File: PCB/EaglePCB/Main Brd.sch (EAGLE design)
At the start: 9 parts, among them J1 1909763-1, J2 1909763-1, U1 ATWINC1500-MR210PB1952-T, U2 ENC28J60-I/SP, U3 MSP430FR2355TDBTRDBT0038A_M, U4 SX1272IMLTRT, U5 SX1272IMLTRT, U6 ARJM11C7-114-BA-EW2

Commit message: LoRa Antenna + Ethernet routing
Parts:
- removed J2: 1909763-1, 473:1909763-1
- added 10NH-ANT1, 10NH-ANT2, C1: (no value), microbuilder:CAP_CERAMIC0402
- added ANT1-ANT2\, ANT1-ANT2\1: 8.2nH, microbuilder:INDUCTOR_0402
- added ANT1-GND, ANT1-GND1, ANT2-GND, ANT2-GND1, ANT2-GND2, ANT2-GND3: 4.7pF, microbuilder:CAP_CERAMIC0402
- added ANT2-ANT1, ANT2-ANT3: 7.5nH, microbuilder:INDUCTOR_0402
- added J3: 1909763-1, 473:1909763-1
- added L2: (no value), microbuilder:INDUCTOR_0402
- added R1: (no value), microbuilder:RESISTOR0402
- added RFI-GND, RFI-GND1: 5.6 nH, microbuilder:INDUCTOR_0402
- added RFI-RFO, RFI-RFO1: 1.5pF 50v Cer, microbuilder:CAP_CERAMIC0402
- added RFO-33PF, RFO-33PF1: 10nH, microbuilder:INDUCTOR_0402
- added RFO-VR_PA, RFO-VR_PA1, VR_PA-PA_BOOST, VR_PA-PA_BOOST1: 33nH, microbuilder:INDUCTOR_0402
- renumbered U4 to LORA2, U5 to LORA1
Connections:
- new net ANT1: 10NH-ANT1.P$1, ANT1-ANT2\.2, ANT1-GND.P$2
- new net ANT1-2: 10NH-ANT2.P$1, ANT1-ANT2\1.2, ANT1-GND1.P$2
- new net ANT2: ANT1-ANT2\.1, ANT2-ANT3.2, ANT2-GND.P$2
- new net ANT2-2: ANT1-ANT2\1.1, ANT2-ANT1.2, ANT2-GND2.P$2
- new net ANT3: ANT2-ANT3.1, ANT2-GND1.P$2, J1.SIG
- new net ANT3-2: ANT2-ANT1.1, ANT2-GND3.P$2, J3.SIG
- new net GND: ANT1-GND.P$1, ANT1-GND1.P$1, ANT2-GND.P$1, ANT2-GND1.P$1, ANT2-GND2.P$1, ANT2-GND3.P$1, J1.GND, J1.GND_2, J3.GND, J3.GND_2, LORA1.GND, LORA1.GND_2, LORA1.GND_3, LORA1.GND_4, LORA2.GND, LORA2.GND_2, LORA2.GND_3, LORA2.GND_4, RFI-GND.2, RFI-GND1.2
- new net N$1: 10NH-ANT1.P$2, RFO-33PF.1
- new net N$2: 10NH-ANT2.P$2, RFO-33PF1.1
- new net PA_BOOST: LORA1.PA_BOOST, VR_PA-PA_BOOST.1
- new net PA_BOOST2: LORA2.PA_BOOST, VR_PA-PA_BOOST1.1
- new net RFI: LORA1.RFI, RFI-GND.1, RFI-RFO.P$1
- new net RFI2: LORA2.RFI, RFI-GND1.1, RFI-RFO1.P$1
- new net RFO: LORA1.RFO, RFI-RFO.P$2, RFO-33PF.2, RFO-VR_PA.2
- new net RFO2: LORA2.RFO, RFI-RFO1.P$2, RFO-33PF1.2, RFO-VR_PA1.2
- new net VR_PA: LORA1.VR_PA, RFO-VR_PA.1, VR_PA-PA_BOOST.2
- new net VR_PA2: LORA2.VR_PA, RFO-VR_PA1.1, VR_PA-PA_BOOST1.2
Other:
- moved on the sheet: J1, U1

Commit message: updated ethernet
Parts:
- added LEDG, LEDY: (no value), microbuilder:RESISTOR0402
- added RD-GND, RD-GND1: 0.1 uF, microbuilder:CAP_CERAMIC0402
- added RDM-GND, RDM-GND1: 49.9 Ohm', microbuilder:RESISTOR0402
- added RDP-GND, RDP-GND1: 49.9 Ohm, microbuilder:RESISTOR0402
- added TCT-3V3: (no value), microbuilder:FERRITE
- added U$1: NC_MARKER, NC_MARKER:NC_MARKER
- added VC2ETH-GND, VC2PETH-GND: 75 Ohm, microbuilder:RESISTOR0402
- added VC2ETH-GNDC, VC2PETH-GNDC: 1nF, microbuilder:CAP_CERAMIC0402
- added VCAPCLOSE: 10 uF, microbuilder:CAP_CERAMIC0805
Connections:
- new net 3V3: LEDG.2, LEDY.2, TCT-3V3.P$2
- new net LEDGN: U2.LEDA, U6.LED_3
- new net LEDYN: U6.LED
- new net LEDYP: U2.LEDB
- new net N$3: U$1.P$1, U6.RCT
- new net N$4: U2.VCAP, VCAPCLOSE.P$2
- new net N$5: VC2ETH-GND.1, VC2ETH-GNDC.P$2
- new net N$6: VC2PETH-GND.1, VC2PETH-GNDC.P$2
- new net N$7: LEDY.1, U6.LED_4
- new net N$8: RD-GND.P$1, RDM-GND.1, RDP-GND.1
- new net N$9: LEDG.1, U6.LED_2
- new net RDM: RDM-GND.2, U2.TPIN-, U6.RD-
- new net RDP: RDP-GND.2, U2.TPIN+, U6.RD+
- new net TDC: RD-GND1.P$1, RDM-GND1.1, RDP-GND1.1, TCT-3V3.P$1, U6.TCT
- new net TDM: RDM-GND1.2, U2.TPOUT-, U6.TD-
- new net TDP: RDP-GND1.2, U2.TPOUT+, U6.TD+
- new net VC2ETH: U6.VC2-, VC2ETH-GND.2
- new net VC2PETH: U6.VC2+, VC2PETH-GND.2
- net GND: now also RD-GND.P$2, RD-GND1.P$2, U6.VC1+, U6.VC1-, VC2ETH-GNDC.P$1, VC2PETH-GNDC.P$1, VCAPCLOSE.P$1
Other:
- moved on the sheet: U6

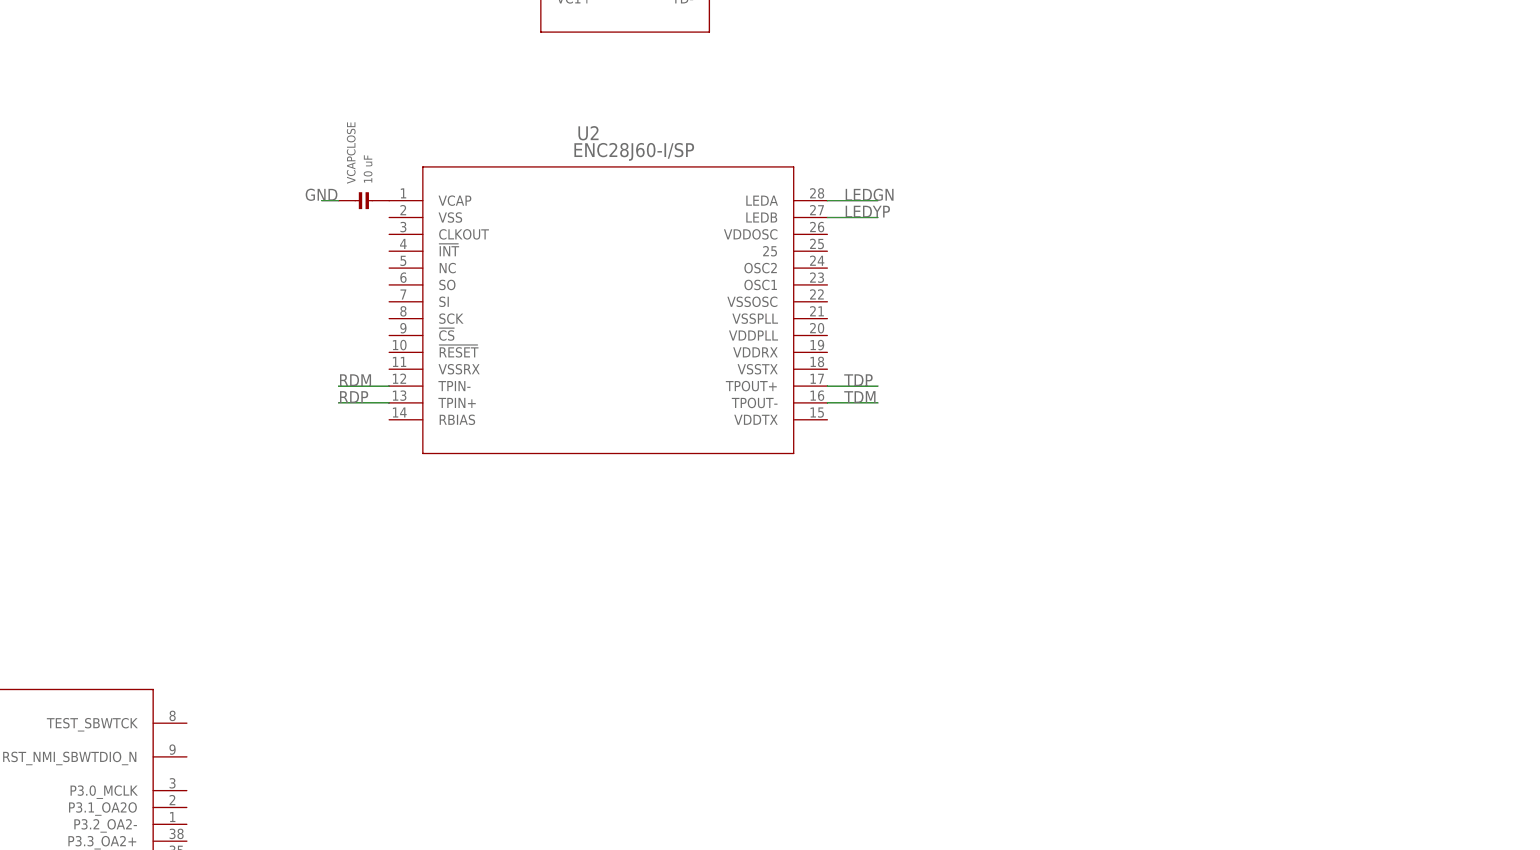
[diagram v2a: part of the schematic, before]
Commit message: added eth power coupling and Osc circuit
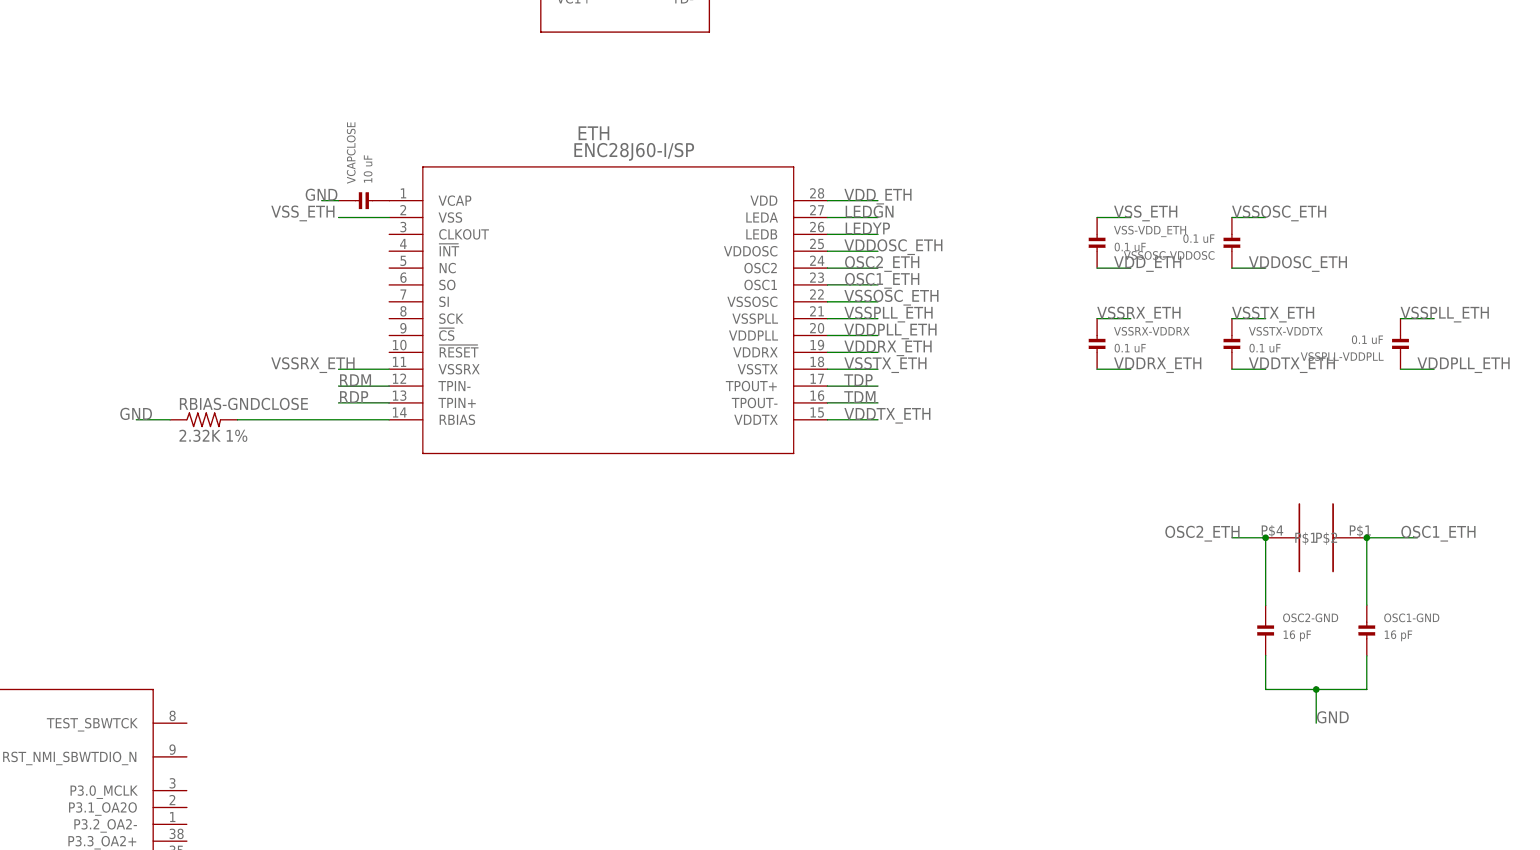
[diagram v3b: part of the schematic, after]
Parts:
- added OSC1-GND, OSC2-GND: 16 pF, microbuilder:CAP_CERAMIC0603
- added RBIAS-GNDCLOSE: 2.32K 1%, Resistor_Capacitor:RC0603JR-070RL
- added U$2: CRYSTAL, 473:CRYSTAL
- added VSS-VDD_ETH, VSSOSC-VDDOSC, VSSPLL-VDDPLL, VSSRX-VDDRX, VSSTX-VDDTX: 0.1 uF, microbuilder:CAP_CERAMIC0603
- RD-GND, RD-GND1: device microbuilder:CAP_CERAMIC0402 -> microbuilder:CAP_CERAMIC0603
- renumbered U2 to ETH
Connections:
- new net N$10: ETH.RBIAS, RBIAS-GNDCLOSE.2
- new net OSC1_ETH: ETH.OSC1, OSC1-GND.P$1, U$2.P$1
- new net OSC2_ETH: ETH.OSC2, OSC2-GND.P$1, U$2.P$2
- new net VDDOSC_ETH: ETH.VDDOSC, VSSOSC-VDDOSC.P$1
- new net VDDPLL_ETH: ETH.VDDPLL, VSSPLL-VDDPLL.P$1
- new net VDDRX_ETH: ETH.VDDRX, VSSRX-VDDRX.P$2
- new net VDDTX_ETH: ETH.VDDTX, VSSTX-VDDTX.P$2
- new net VDD_ETH: ETH.VDD, VSS-VDD_ETH.P$2
- new net VSSOSC_ETH: ETH.VSSOSC, VSSOSC-VDDOSC.P$2
- new net VSSPLL_ETH: ETH.VSSPLL, VSSPLL-VDDPLL.P$2
- new net VSSRX_ETH: ETH.VSSRX, VSSRX-VDDRX.P$1
- new net VSSTX_ETH: ETH.VSSTX, VSSTX-VDDTX.P$1
- new net VSS_ETH: ETH.VSS, VSS-VDD_ETH.P$1
- net GND: now also OSC1-GND.P$2, OSC2-GND.P$2, RBIAS-GNDCLOSE.1

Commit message: removed LED group
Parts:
- removed D1: 5700100132F, 473:5700100132F
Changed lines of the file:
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@@
 <part name="U3" library="473" deviceset="MSP430FR2355TDBTR" device="DBT0038A_M"/>
 <part name="LORA2" library="473" deviceset="SX1272IMLTRT" device=""/>
-<part name="D1" library="473" deviceset="5700100132F" device=""/>
 <part name="LORA1" library="473" deviceset="SX1272IMLTRT" device=""/>
 <part name="U6" library="473" deviceset="ARJM11C7-114-BA-EW2" device=""/>
@@
 <attribute name="VALUE" x="-56.1594" y="52.2986" size="2.0828" layer="96" ratio="6" rot="SR0"/>
 </instance>
-<instance part="D1" gate="G$1" x="134.62" y="66.04" smashed="yes">
-<attribute name="NAME" x="127" y="82.042" size="1.778" layer="95"/>
-<attribute name="VALUE" x="127" y="50.038" size="1.778" layer="96" align="top-left"/>
-</instance>
 <instance part="LORA1" gate="A" x="-76.2" y="101.6" smashed="yes">

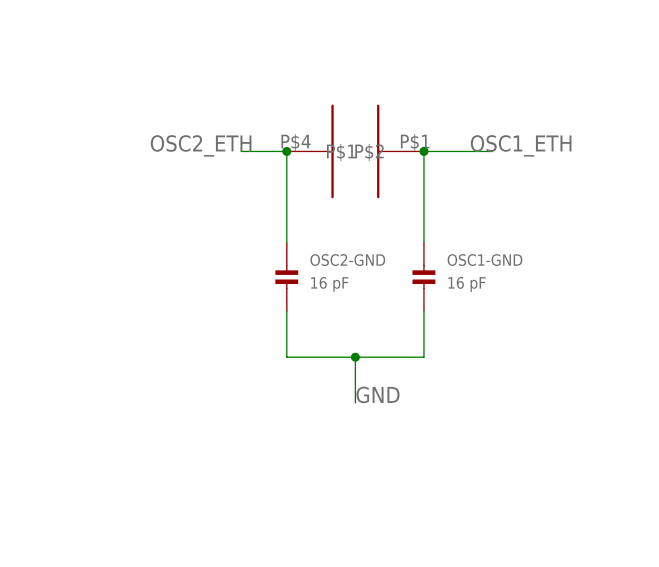
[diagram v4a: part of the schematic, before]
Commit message: adjusted crystal oscillator values
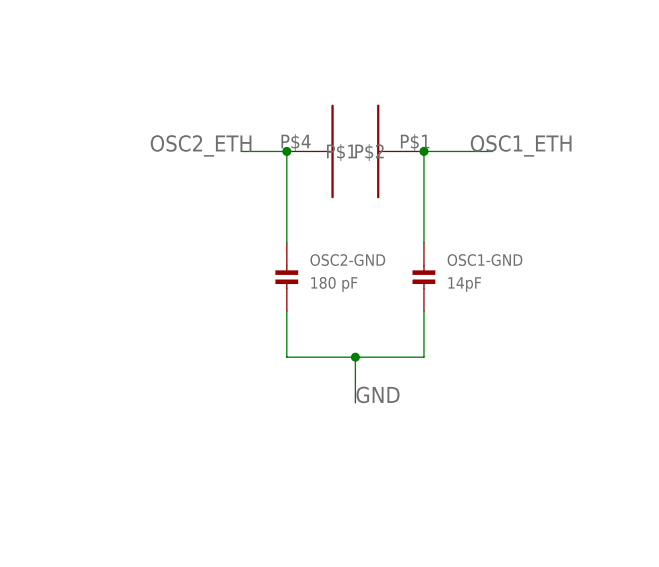
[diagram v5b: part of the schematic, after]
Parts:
- OSC1-GND: value 16 pF -> 14pF
- OSC2-GND: value 16 pF -> 180 pF
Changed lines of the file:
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@@
 <part name="VSSPLL-VDDPLL" library="microbuilder" deviceset="CAP_CERAMIC" device="0603" value="0.1 uF"/>
 <part name="U$2" library="473" deviceset="CRYSTAL" device=""/>
-<part name="OSC2-GND" library="microbuilder" deviceset="CAP_CERAMIC" device="0603" value="16 pF"/>
-<part name="OSC1-GND" library="microbuilder" deviceset="CAP_CERAMIC" device="0603" value="16 pF"/>
+<part name="OSC2-GND" library="microbuilder" deviceset="CAP_CERAMIC" device="0603" value="180 pF"/>
+<part name="OSC1-GND" library="microbuilder" deviceset="CAP_CERAMIC" device="0603" value="14pF"/>
 </parts>
 <sheets>

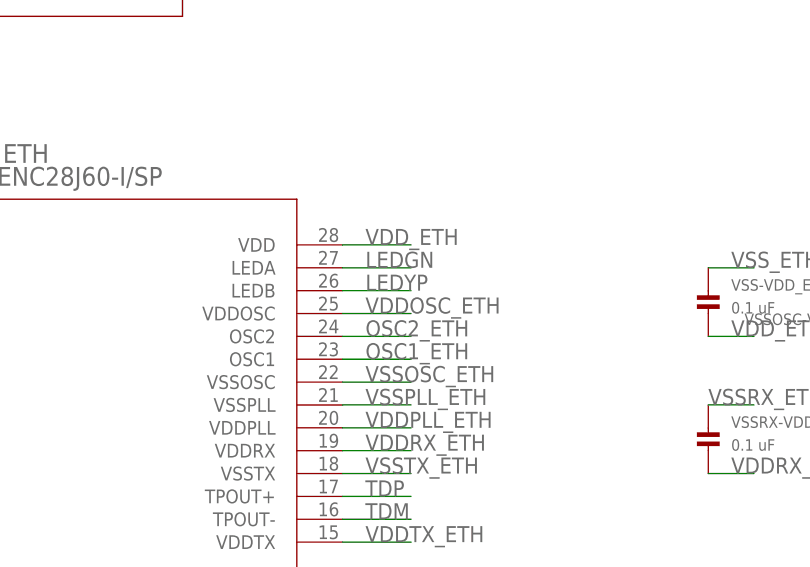
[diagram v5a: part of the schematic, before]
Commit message: edited ethernet with minor routing
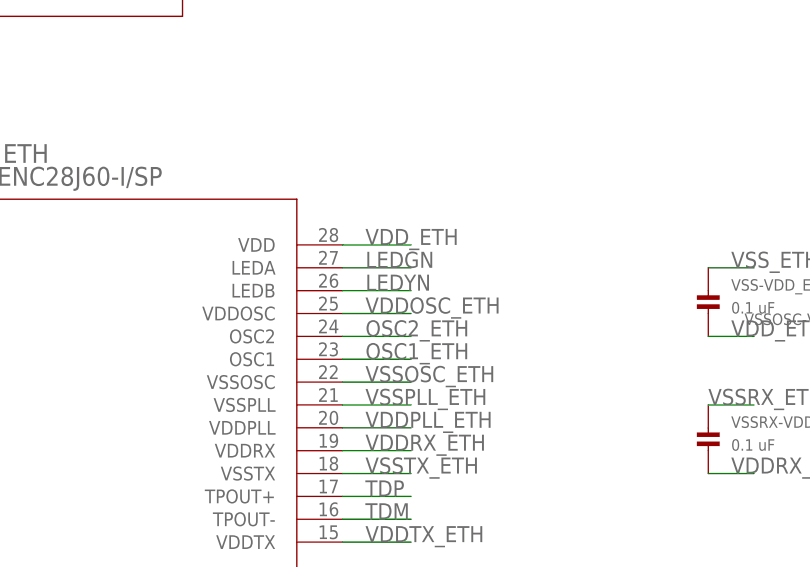
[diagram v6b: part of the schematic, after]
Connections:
- removed net LEDYP: ETH.LEDB
- net LEDYN: now also ETH.LEDB
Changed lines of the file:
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@@
 <grid distance="0.1" unitdist="inch" unit="inch" style="lines" multiple="1" display="no" altdistance="0.01" altunitdist="inch" altunit="inch"/>
 <layers>
-<layer number="1" name="Top" color="4" fill="1" visible="yes" active="no"/>
-<layer number="16" name="Bottom" color="1" fill="1" visible="yes" active="no"/>
-<layer number="17" name="Pads" color="2" fill="1" visible="yes" active="no"/>
-<layer number="18" name="Vias" color="2" fill="1" visible="yes" active="no"/>
-<layer number="19" name="Unrouted" color="6" fill="1" visible="yes" active="no"/>
-<layer number="20" name="Dimension" color="24" fill="1" visible="yes" active="no"/>
-<layer number="21" name="tPlace" color="7" fill="1" visible="yes" active="no"/>
-<layer number="22" name="bPlace" color="7" fill="1" visible="yes" active="no"/>
-<layer number="23" name="tOrigins" color="15" fill="1" visible="yes" active="no"/>
-<layer number="24" name="bOrigins" color="15" fill="1" visible="yes" active="no"/>
-<layer number="25" name="tNames" color="7" fill="1" visible="yes" active="no"/>
-<layer number="26" name="bNames" color="7" fill="1" visible="yes" active="no"/>
-<layer number="27" name="tValues" color="7" fill="1" visible="yes" active="no"/>
-<layer number="28" name="bValues" color="7" fill="1" visible="yes" active="no"/>
+<layer number="1" name="Top" color="4" fill="1" visible="no" active="no"/>
+<layer number="16" name="Bottom" color="1" fill="1" visible="no" active="no"/>
+<layer number="17" name="Pads" color="2" fill="1" visible="no" active="no"/>
+<layer number="18" name="Vias" color="2" fill="1" visible="no" active="no"/>
+<layer number="19" name="Unrouted" color="6" fill="1" visible="no" active="no"/>
+<layer number="20" name="Dimension" color="24" fill="1" visible="no" active="no"/>
+<layer number="21" name="tPlace" color="7" fill="1" visible="no" active="no"/>
+<layer number="22" name="bPlace" color="7" fill="1" visible="no" active="no"/>
+<layer number="23" name="tOrigins" color="15" fill="1" visible="no" active="no"/>
+<layer number="24" name="bOrigins" color="15" fill="1" visible="no" active="no"/>
+<layer number="25" name="tNames" color="7" fill="1" visible="no" active="no"/>
+<layer number="26" name="bNames" color="7" fill="1" visible="no" active="no"/>
+<layer number="27" name="tValues" color="7" fill="1" visible="no" active="no"/>
+<layer number="28" name="bValues" color="7" fill="1" visible="no" active="no"/>
 <layer number="29" name="tStop" color="7" fill="3" visible="no" active="no"/>
 <layer number="30" name="bStop" color="7" fill="6" visible="no" active="no"/>
@@
 <layer number="35" name="tGlue" color="7" fill="4" visible="no" active="no"/>
 <layer number="36" name="bGlue" color="7" fill="5" visible="no" active="no"/>
-<layer number="37" name="tTest" color="7" fill="1" visible="yes" active="no"/>
-<layer number="38" name="bTest" color="7" fill="1" visible="yes" active="no"/>
+<layer number="37" name="tTest" color="7" fill="1" visible="no" active="no"/>
+<layer number="38" name="bTest" color="7" fill="1" visible="no" active="no"/>
 <layer number="39" name="tKeepout" color="4" fill="11" visible="no" active="no"/>
 <layer number="40" name="bKeepout" color="1" fill="11" visible="no" active="no"/>
@@
 <layer number="44" name="Drills" color="7" fill="1" visible="no" active="no"/>
 <layer number="45" name="Holes" color="7" fill="1" visible="no" active="no"/>
-<layer number="46" name="Milling" color="3" fill="1" visible="yes" active="no"/>
-<layer number="47" name="Measures" color="7" fill="1" visible="yes" active="no"/>
-<layer number="48" name="Document" color="7" fill="1" visible="yes" active="no"/>
-<layer number="49" name="Reference" color="7" fill="1" visible="yes" active="no"/>
-<layer number="50" name="dxf" color="7" fill="1" visible="yes" active="no"/>
-<layer number="51" name="tDocu" color="7" fill="1" visible="yes" active="no"/>
-<layer number="52" name="bDocu" color="7" fill="1" visible="yes" active="no"/>
-<layer number="53" name="tGND_GNDA" color="7" fill="9" visible="yes" active="no"/>
-<layer number="54" name="bGND_GNDA" color="1" fill="9" visible="yes" active="no"/>
-<layer number="56" name="wert" color="7" fill="1" visible="yes" active="no"/>
-<layer number="57" name="tCAD" color="7" fill="1" visible="yes" active="no"/>
-<layer number="59" name="tCarbon" color="7" fill="1" visible="yes" active="no"/>
-<layer number="60" name="bCarbon" color="7" fill="1" visible="yes" active="no"/>
+<layer number="46" name="Milling" color="3" fill="1" visible="no" active="no"/>
+<layer number="47" name="Measures" color="7" fill="1" visible="no" active="no"/>
+<layer number="48" name="Document" color="7" fill="1" visible="no" active="no"/>
+<layer number="49" name="Reference" color="7" fill="1" visible="no" active="no"/>
+<layer number="50" name="dxf" color="7" fill="1" visible="no" active="no"/>
+<layer number="51" name="tDocu" color="7" fill="1" visible="no" active="no"/>
+<layer number="52" name="bDocu" color="7" fill="1" visible="no" active="no"/>
+<layer number="53" name="tGND_GNDA" color="7" fill="9" visible="no" active="no"/>
+<layer number="54" name="bGND_GNDA" color="1" fill="9" visible="no" active="no"/>
+<layer number="56" name="wert" color="7" fill="1" visible="no" active="no"/>
+<layer number="57" name="tCAD" color="7" fill="1" visible="no" active="no"/>
+<layer number="59" name="tCarbon" color="7" fill="1" visible="no" active="no"/>
+<layer number="60" name="bCarbon" color="7" fill="1" visible="no" active="no"/>
 <layer number="88" name="SimResults" color="9" fill="1" visible="yes" active="yes"/>
 <layer number="89" name="SimProbes" color="9" fill="1" visible="yes" active="yes"/>
@@
 <label x="271.78" y="93.98" size="1.778" layer="95"/>
 </segment>
+<segment>
+<pinref part="ETH" gate="A" pin="LEDB"/>
+<wire x1="279.4" y1="43.18" x2="287.02" y2="43.18" width="0.1524" layer="91"/>
+<label x="281.94" y="43.18" size="1.778" layer="95"/>
+</segment>
 </net>
 <net name="LEDGN" class="0">
@@
 </segment>
 </net>
-<net name="LEDYP" class="0">
-<segment>
-<pinref part="ETH" gate="A" pin="LEDB"/>
-<wire x1="279.4" y1="43.18" x2="287.02" y2="43.18" width="0.1524" layer="91"/>
-<label x="281.94" y="43.18" size="1.778" layer="95"/>
-</segment>
-</net>
